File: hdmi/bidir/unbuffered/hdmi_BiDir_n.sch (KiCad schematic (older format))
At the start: 32 parts

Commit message: Adding some text notes.
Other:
- note added: "5V HDMI Supply"
- note added: "Hot plug drive or detect"
- note added: "I2C / EDID Level Shifter"
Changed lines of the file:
@@
 LIBS:contrib
 LIBS:valves
+LIBS:pmod-conn_6x2
+LIBS:hdmi
 LIBS:hdmi_BiDir_n
 LIBS:hdmi_BiDir_n-cache
@@
 Text HLabel 2600 6600 0    60   BiDi ~ 0
 HDMI_SDA
+Text Notes 7020 715  0    60   ~ 0
+Hot plug drive or detect
+Text Notes 5155 4495 0    60   ~ 0
+5V HDMI Supply
+Text Notes 4085 6960 0    60   ~ 0
+I2C / EDID Level Shifter
 $EndSCHEMATC

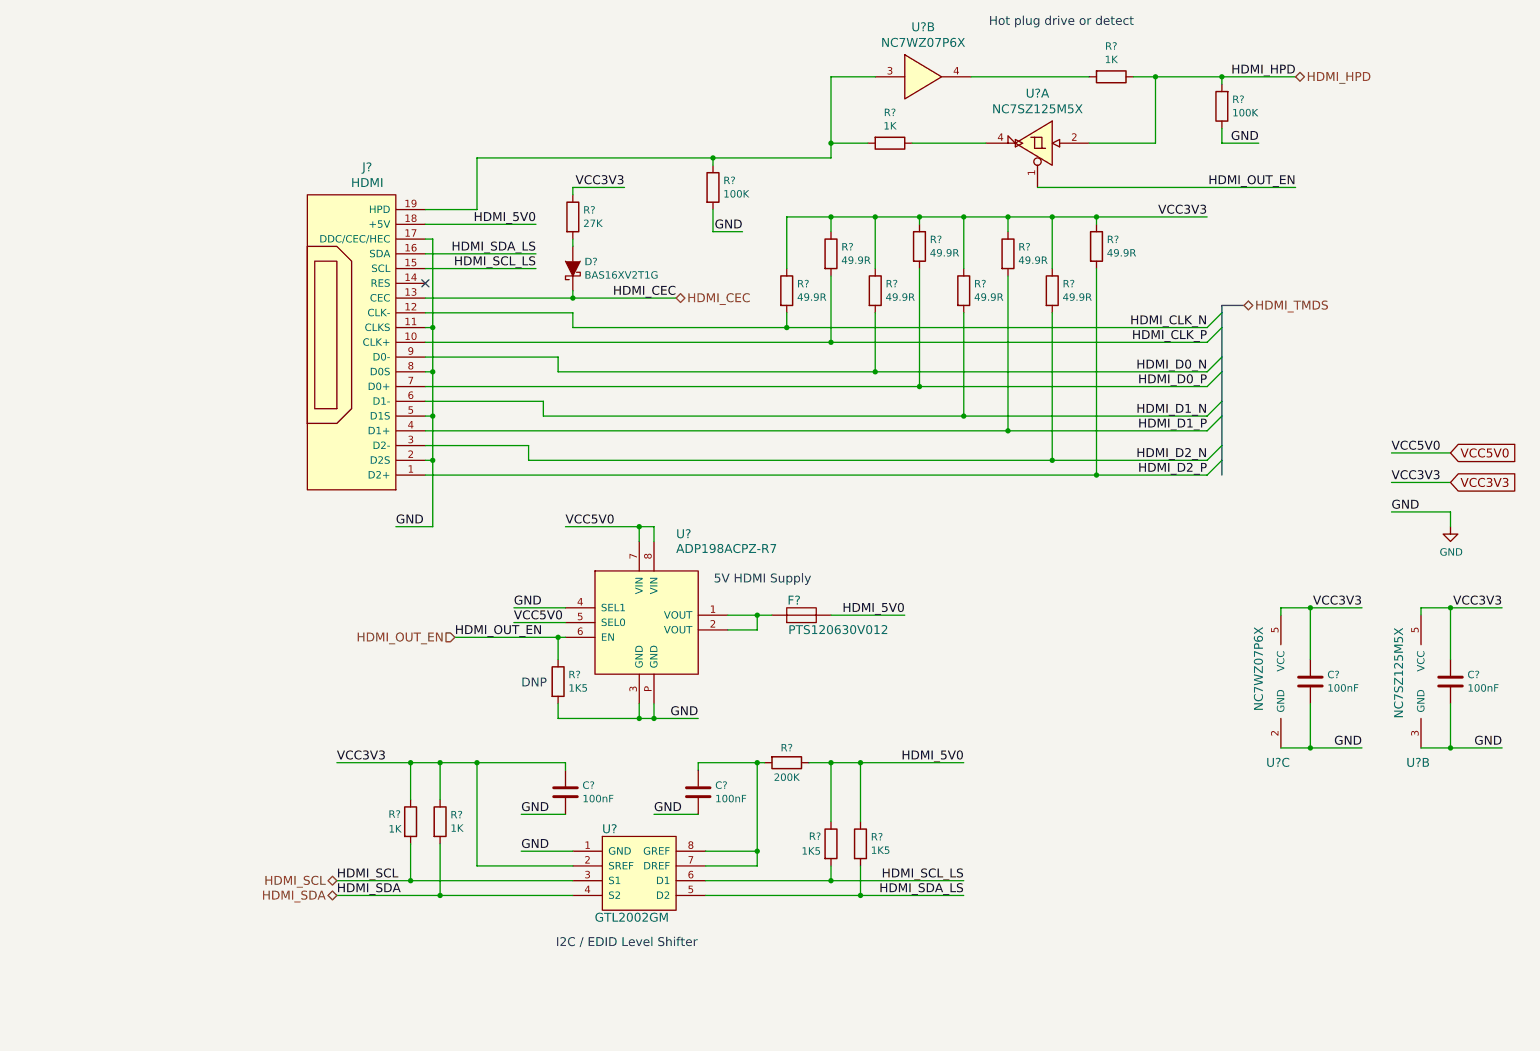
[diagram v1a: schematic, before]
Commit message: Starting templetization.
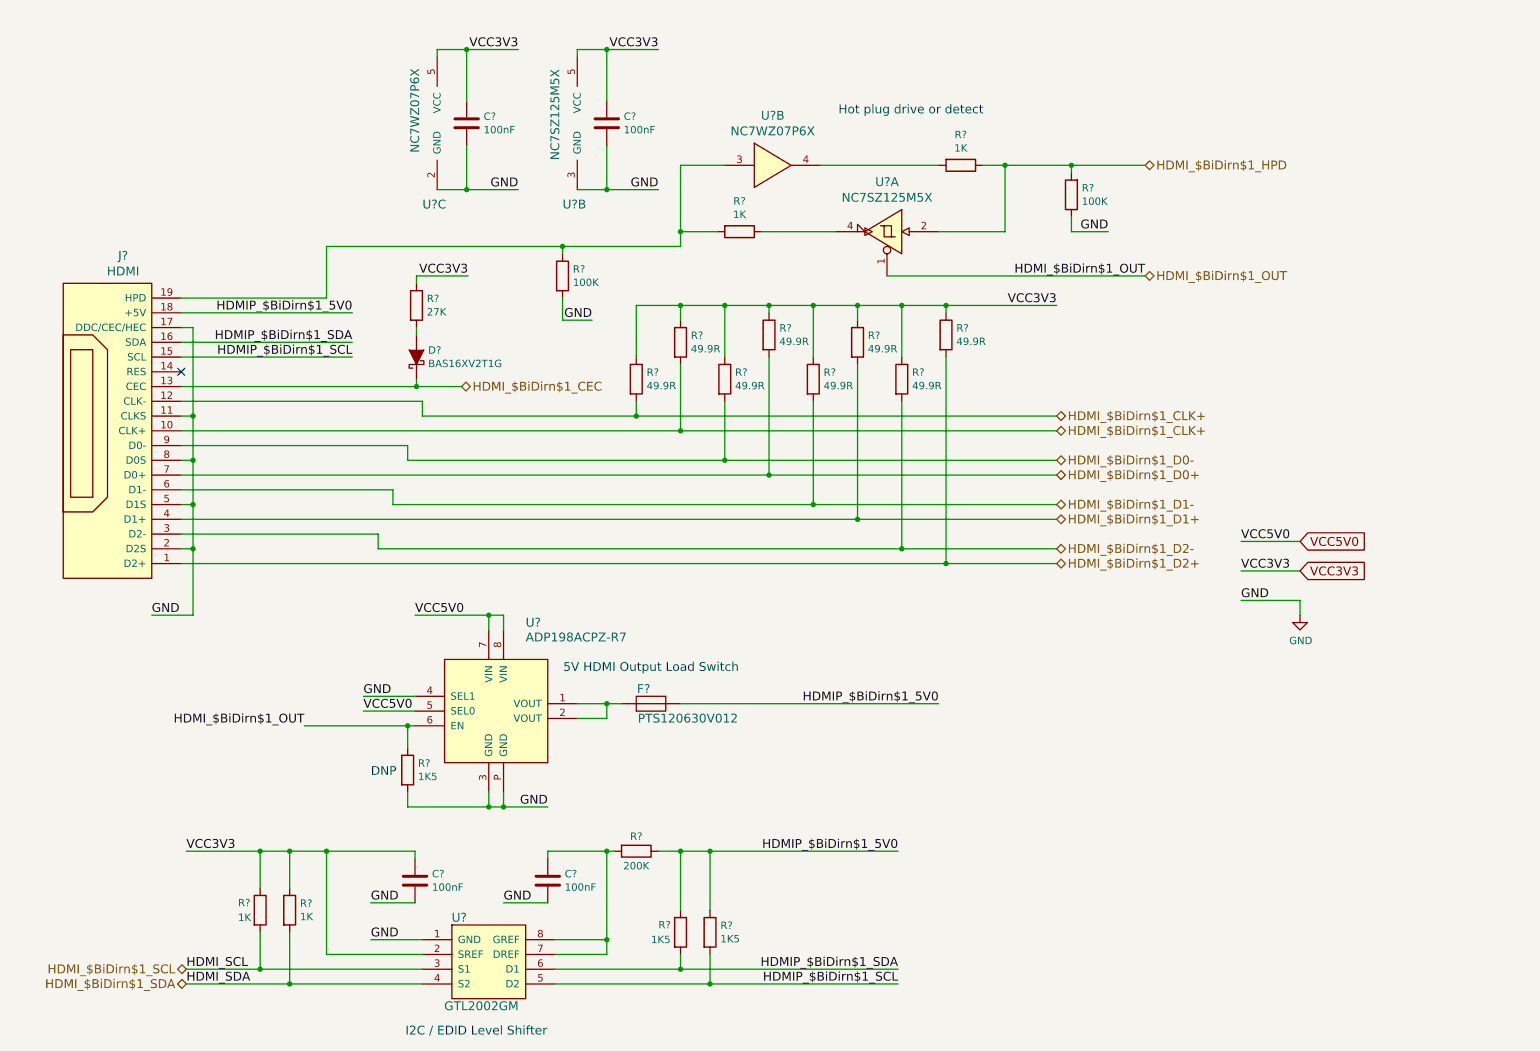
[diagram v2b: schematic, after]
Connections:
- net HDMI_CLK_P is gone; now on net HDMI_$BiDirn$1_CLK+: J?.10 (CLK+), R?.2
- net HDMI_5V0 renamed HDMIP_$BiDirn$1_5V0
- net HDMI_CEC renamed HDMI_$BiDirn$1_CEC
- net HDMI_CLK_N renamed HDMI_$BiDirn$1_CLK+
- net HDMI_D0_N renamed HDMI_$BiDirn$1_D0-
- net HDMI_D0_P renamed HDMI_$BiDirn$1_D0+
- net HDMI_D1_N renamed HDMI_$BiDirn$1_D1-
- net HDMI_D1_P renamed HDMI_$BiDirn$1_D1+
- net HDMI_D2_N renamed HDMI_$BiDirn$1_D2-
- net HDMI_D2_P renamed HDMI_$BiDirn$1_D2+
- net HDMI_HPD renamed HDMI_$BiDirn$1_HPD
- net HDMI_OUT_EN renamed HDMI_$BiDirn$1_OUT
- net HDMI_SCL renamed HDMI_$BiDirn$1_SCL
- net HDMI_SCL_LS renamed HDMIP_$BiDirn$1_SDA
- net HDMIP_$BiDirn$1_SDA: now also J?.16 (SDA); no longer J?.15 (SCL)
- net HDMI_SDA renamed HDMI_$BiDirn$1_SDA
- net HDMI_SDA_LS renamed HDMIP_$BiDirn$1_SCL
- net HDMIP_$BiDirn$1_SCL: now also J?.15 (SCL); no longer J?.16 (SDA)
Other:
- note added: "5V HDMI Output Load Switch"
- note removed: "5V HDMI Supply"
- moved on the sheet: C?, D?, F?, J?, R?, U?, U?A, U?B, U?C

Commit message: Using the new HDMI parts.
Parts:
- J?: value HDMI -> HDMI_BIDIR; symbol HDMI -> HDMI_BIDIR
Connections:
- net labels added: HDMI_$BiDirn$1_CLK-
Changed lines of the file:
@@
 $EndDescr
 $Comp
-L HDMI J?
+L HDMI_BIDIR J?
 U 1 1 57E7C395
 P 995 3450
 F 0 "J?" H 839 2263 60  0000 C CNN
-F 1 "HDMI" H 839 2369 60  0000 C CNN
+F 1 "HDMI_BIDIR" H 839 2369 60  0000 C CNN
 F 2 "" H 945 3450 60  0000 C CNN
 F 3 "" H 945 3450 60  0000 C CNN
@@
 I2C / EDID Level Shifter
 Text HLabel 7480 3350 2    60   BiDi ~ 0
-HDMI_$BiDirn$1_CLK+
+HDMI_$BiDirn$1_CLK-
 Text HLabel 7480 3450 2    60   BiDi ~ 0
 HDMI_$BiDirn$1_CLK+
